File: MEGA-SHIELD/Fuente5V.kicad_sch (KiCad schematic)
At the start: 11 parts, among them J1 12V

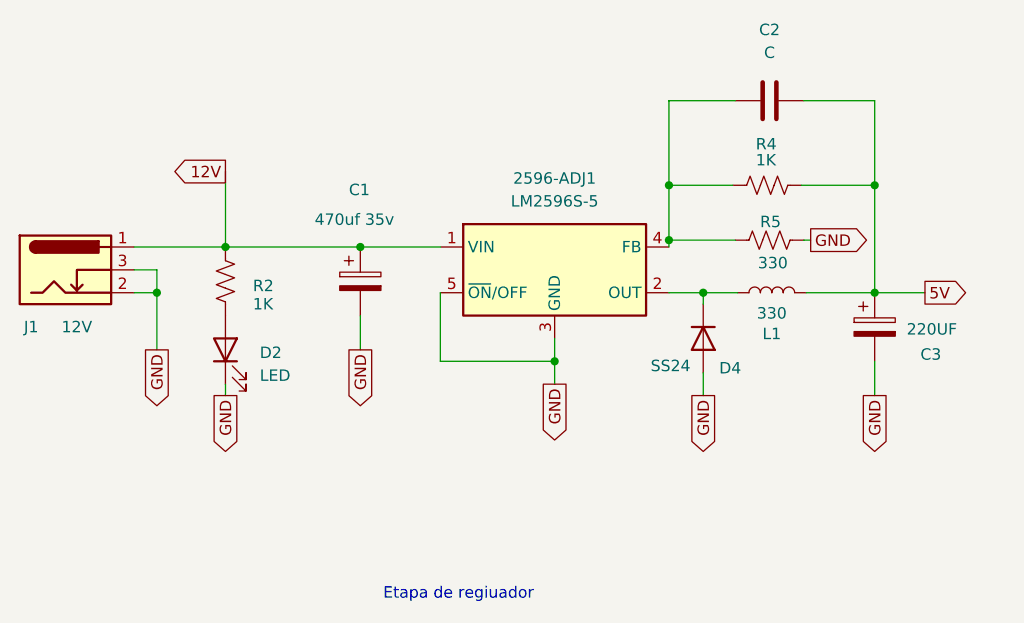
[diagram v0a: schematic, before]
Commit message: feat: agrege reles y optos
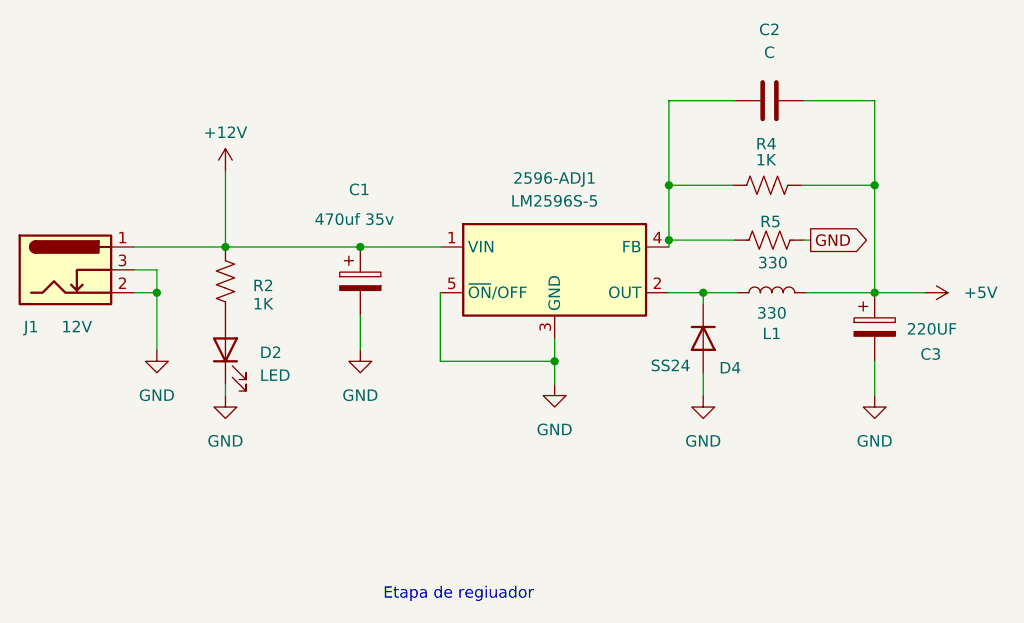
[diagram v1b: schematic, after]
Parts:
- 2596-ADJ1: footprint Package_TO_SOT_SMD:TO-263-5_TabPin3 -> TerminalBlock_Phoenix:TerminalBlock_Phoenix_MPT-0,5-3-2.54_1x03_P2.54mm_Horizontal
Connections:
- net 12V renamed +12V
- net 5V renamed +5V
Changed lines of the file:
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@@
     (effects (font (size 1.27 1.27)) (justify left bottom))
-  )
-  (global_label "GND" (shape output) (at 183.134 113.03 270) (fields_autoplaced)
-    (effects (font (size 1.27 1.27)) (justify right))
-    (property "Intersheetrefs" "${INTERSHEET_REFS}" (at 183.134 119.8063 90)
-      (effects (font (size 1.27 1.27)) (justify right) hide)
-    )
-  )
-  (global_label "GND" (shape output) (at 103.378 107.95 270) (fields_autoplaced)
-    (effects (font (size 1.27 1.27)) (justify right))
-    (property "Intersheetrefs" "${INTERSHEET_REFS}" (at 103.378 114.7263 90)
-      (effects (font (size 1.27 1.27)) (justify right) hide)
-    )
-  )
-  (global_label "5V" (shape output) (at 188.722 101.6 0) (fields_autoplaced)
-    (effects (font (size 1.27 1.27)) (justify left))
-    (property "Intersheetrefs" "${INTERSHEET_REFS}" (at 193.9259 101.6 0)
-      (effects (font (size 1.27 1.27)) (justify left) hide)
-    )
-  )
-  (global_label "GND" (shape output) (at 125.984 107.95 270) (fields_autoplaced)
-    (effects (font (size 1.27 1.27)) (justify right))
-    (property "Intersheetrefs" "${INTERSHEET_REFS}" (at 125.984 114.7263 90)
-      (effects (font (size 1.27 1.27)) (justify right) hide)
-    )
-  )
-  (global_label "GND" (shape output) (at 164.084 113.03 270) (fields_autoplaced)
-    (effects (font (size 1.27 1.27)) (justify right))
-    (property "Intersheetrefs" "${INTERSHEET_REFS}" (at 164.084 119.8063 90)
-      (effects (font (size 1.27 1.27)) (justify right) hide)
-    )
   )
   (global_label "GND" (shape output) (at 176.022 95.758 0) (fields_autoplaced)
@@
     )
   )
-  (global_label "GND" (shape output) (at 110.998 113.03 270) (fields_autoplaced)
-    (effects (font (size 1.27 1.27)) (justify right))
-    (property "Intersheetrefs" "${INTERSHEET_REFS}" (at 110.998 119.8063 90)
-      (effects (font (size 1.27 1.27)) (justify right) hide)
-    )
-  )
-  (global_label "GND" (shape output) (at 147.574 111.76 270) (fields_autoplaced)
-    (effects (font (size 1.27 1.27)) (justify right))
-    (property "Intersheetrefs" "${INTERSHEET_REFS}" (at 147.574 118.5363 90)
-      (effects (font (size 1.27 1.27)) (justify right) hide)
-    )
-  )
-  (global_label "12V" (shape output) (at 110.998 88.138 180) (fields_autoplaced)
-    (effects (font (size 1.27 1.27)) (justify right))
-    (property "Intersheetrefs" "${INTERSHEET_REFS}" (at 104.5846 88.138 0)
-      (effects (font (size 1.27 1.27)) (justify right) hide)
-    )
-  )
   (symbol (lib_id "Device:LED") (at 110.998 107.95 90) (unit 1)
     (in_bom yes) (on_board yes) (dnp no)
@@
     )
   )
+  (symbol (lib_id "power:+12V") (at 110.998 88.138 0) (unit 1)
+    (in_bom yes) (on_board yes) (dnp no) (fields_autoplaced)
+    (property "Reference" "#PWR05" (at 110.998 91.948 0)
+      (effects (font (size 1.27 1.27)) hide)
+    )
+    (property "Value" "+12V" (at 110.998 83.82 0)
+      (effects (font (size 1.27 1.27)))
+    )
+    (property "Footprint" "" (at 110.998 88.138 0)
+      (effects (font (size 1.27 1.27)) hide)
+    )
+    (property "Datasheet" "" (at 110.998 88.138 0)
+      (effects (font (size 1.27 1.27)) hide)
+    )
+    (pin "1")
+    (instances
+      (project "ER-PROMEGA-SHIELD"
+        (path "/8147067b-5845-4831-8ba1-364ec5fe594c/5356d373-8a97-48f5-aa7a-74c7e25ebf78"
+          (reference "#PWR05") (unit 1)
+        )
+      )
+    )
+  )
   (symbol (lib_id "Device:C") (at 171.45 80.264 90) (unit 1)
     (in_bom yes) (on_board yes) (dnp no) (fields_autoplaced)
@@
     )
   )
+  (symbol (lib_id "power:GND") (at 110.998 113.03 0) (unit 1)
+    (in_bom yes) (on_board yes) (dnp no) (fields_autoplaced)
+    (property "Reference" "#PWR07" (at 110.998 119.38 0)
+      (effects (font (size 1.27 1.27)) hide)
+    )
+    (property "Value" "GND" (at 110.998 118.11 0)
+      (effects (font (size 1.27 1.27)))
+    )
+    (property "Footprint" "" (at 110.998 113.03 0)
+      (effects (font (size 1.27 1.27)) hide)
+    )
+    (property "Datasheet" "" (at 110.998 113.03 0)
+      (effects (font (size 1.27 1.27)) hide)
+    )
+    (pin "1")
+    (instances
+      (project "ER-PROMEGA-SHIELD"
+        (path "/8147067b-5845-4831-8ba1-364ec5fe594c/5356d373-8a97-48f5-aa7a-74c7e25ebf78"
+          (reference "#PWR07") (unit 1)
+        )
+      )
+    )
+  )
   (symbol (lib_id "Device:R_US") (at 171.196 89.662 270) (unit 1)
     (in_bom yes) (on_board yes) (dnp no)
@@
     )
   )
+  (symbol (lib_id "power:GND") (at 147.574 111.76 0) (unit 1)
+    (in_bom yes) (on_board yes) (dnp no) (fields_autoplaced)
+    (property "Reference" "#PWR09" (at 147.574 118.11 0)
+      (effects (font (size 1.27 1.27)) hide)
+    )
+    (property "Value" "GND" (at 147.574 116.84 0)
+      (effects (font (size 1.27 1.27)))
+    )
+    (property "Footprint" "" (at 147.574 111.76 0)
+      (effects (font (size 1.27 1.27)) hide)
+    )
+    (property "Datasheet" "" (at 147.574 111.76 0)
+      (effects (font (size 1.27 1.27)) hide)
+    )
+    (pin "1")
+    (instances
+      (project "ER-PROMEGA-SHIELD"
+        (path "/8147067b-5845-4831-8ba1-364ec5fe594c/5356d373-8a97-48f5-aa7a-74c7e25ebf78"
+          (reference "#PWR09") (unit 1)
+        )
+      )
+    )
+  )
   (symbol (lib_id "Regulator_Switching:LM2596S-5") (at 147.574 99.06 0) (unit 1)
     (in_bom yes) (on_board yes) (dnp no) (fields_autoplaced)
@@
       (effects (font (size 1.27 1.27)))
     )
-    (property "Footprint" "Package_TO_SOT_SMD:TO-263-5_TabPin3" (at 148.844 105.41 0)
+    (property "Footprint" "TerminalBlock_Phoenix:TerminalBlock_Phoenix_MPT-0,5-3-2.54_1x03_P2.54mm_Horizontal" (at 148.844 105.41 0)
       (effects (font (size 1.27 1.27) italic) (justify left) hide)
     )
@@
     )
   )
+  (symbol (lib_id "power:+5V") (at 188.722 101.6 270) (unit 1)
+    (in_bom yes) (on_board yes) (dnp no) (fields_autoplaced)
+    (property "Reference" "#PWR012" (at 184.912 101.6 0)
+      (effects (font (size 1.27 1.27)) hide)
+    )
+    (property "Value" "+5V" (at 193.04 101.6 90)
+      (effects (font (size 1.27 1.27)) (justify left))
+    )
+    (property "Footprint" "" (at 188.722 101.6 0)
+      (effects (font (size 1.27 1.27)) hide)
+    )
+    (property "Datasheet" "" (at 188.722 101.6 0)
+      (effects (font (size 1.27 1.27)) hide)
+    )
+    (pin "1")
+    (instances
+      (project "ER-PROMEGA-SHIELD"
+        (path "/8147067b-5845-4831-8ba1-364ec5fe594c/5356d373-8a97-48f5-aa7a-74c7e25ebf78"
+          (reference "#PWR012") (unit 1)
+        )
+      )
+    )
+  )
+  (symbol (lib_id "power:GND") (at 125.984 107.95 0) (unit 1)
+    (in_bom yes) (on_board yes) (dnp no) (fields_autoplaced)
+    (property "Reference" "#PWR08" (at 125.984 114.3 0)
+      (effects (font (size 1.27 1.27)) hide)
+    )
+    (property "Value" "GND" (at 125.984 113.03 0)
+      (effects (font (size 1.27 1.27)))
+    )
+    (property "Footprint" "" (at 125.984 107.95 0)
+      (effects (font (size 1.27 1.27)) hide)
+    )
+    (property "Datasheet" "" (at 125.984 107.95 0)
+      (effects (font (size 1.27 1.27)) hide)
+    )
+    (pin "1")
+    (instances
+      (project "ER-PROMEGA-SHIELD"
+        (path "/8147067b-5845-4831-8ba1-364ec5fe594c/5356d373-8a97-48f5-aa7a-74c7e25ebf78"
+          (reference "#PWR08") (unit 1)
+        )
+      )
+    )
+  )
+  (symbol (lib_id "power:GND") (at 103.378 107.95 0) (unit 1)
+    (in_bom yes) (on_board yes) (dnp no) (fields_autoplaced)
+    (property "Reference" "#PWR06" (at 103.378 114.3 0)
+      (effects (font (size 1.27 1.27)) hide)
+    )
+    (property "Value" "GND" (at 103.378 113.03 0)
+      (effects (font (size 1.27 1.27)))
+    )
+    (property "Footprint" "" (at 103.378 107.95 0)
+      (effects (font (size 1.27 1.27)) hide)
+    )
+    (property "Datasheet" "" (at 103.378 107.95 0)
+      (effects (font (size 1.27 1.27)) hide)
+    )
+    (pin "1")
+    (instances
+      (project "ER-PROMEGA-SHIELD"
+        (path "/8147067b-5845-4831-8ba1-364ec5fe594c/5356d373-8a97-48f5-aa7a-74c7e25ebf78"
+          (reference "#PWR06") (unit 1)
+        )
+      )
+    )
+  )
+  (symbol (lib_id "power:GND") (at 164.084 113.03 0) (unit 1)
+    (in_bom yes) (on_board yes) (dnp no) (fields_autoplaced)
+    (property "Reference" "#PWR010" (at 164.084 119.38 0)
+      (effects (font (size 1.27 1.27)) hide)
+    )
+    (property "Value" "GND" (at 164.084 118.11 0)
+      (effects (font (size 1.27 1.27)))
+    )
+    (property "Footprint" "" (at 164.084 113.03 0)
+      (effects (font (size 1.27 1.27)) hide)
+    )
+    (property "Datasheet" "" (at 164.084 113.03 0)
+      (effects (font (size 1.27 1.27)) hide)
+    )
+    (pin "1")
+    (instances
+      (project "ER-PROMEGA-SHIELD"
+        (path "/8147067b-5845-4831-8ba1-364ec5fe594c/5356d373-8a97-48f5-aa7a-74c7e25ebf78"
+          (reference "#PWR010") (unit 1)
+        )
+      )
+    )
+  )
   (symbol (lib_id "Device:C_Polarized") (at 183.134 105.41 0) (unit 1)
     (in_bom yes) (on_board yes) (dnp no)
@@
         )
       )
+    )
+  )
+  (symbol (lib_id "power:GND") (at 183.134 113.03 0) (unit 1)
+    (in_bom yes) (on_board yes) (dnp no) (fields_autoplaced)
+    (property "Reference" "#PWR011" (at 183.134 119.38 0)
+      (effects (font (size 1.27 1.27)) hide)
+    )
+    (property "Value" "GND" (at 183.134 118.11 0)
+      (effects (font (size 1.27 1.27)))
+    )
+    (property "Footprint" "" (at 183.134 113.03 0)
+      (effects (font (size 1.27 1.27)) hide)
+    )
+    (property "Datasheet" "" (at 183.134 113.03 0)
+      (effects (font (size 1.27 1.27)) hide)
+    )
+    (pin "1")
+    (instances
+      (project "ER-PROMEGA-SHIELD"
+        (path "/8147067b-5845-4831-8ba1-364ec5fe594c/5356d373-8a97-48f5-aa7a-74c7e25ebf78"
+          (reference "#PWR011") (unit 1)
+        )
+      )

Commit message: feat: avances2
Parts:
- 2596-ADJ1: footprint TerminalBlock_Phoenix:TerminalBlock_Phoenix_MPT-0,5-3-2.54_1x03_P2.54mm_Horizontal -> Package_TO_SOT_SMD:TO-263-5_TabPin3
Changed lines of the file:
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@@
       (effects (font (size 1.27 1.27)))
     )
-    (property "Footprint" "TerminalBlock_Phoenix:TerminalBlock_Phoenix_MPT-0,5-3-2.54_1x03_P2.54mm_Horizontal" (at 148.844 105.41 0)
+    (property "Footprint" "Package_TO_SOT_SMD:TO-263-5_TabPin3" (at 148.844 105.41 0)
       (effects (font (size 1.27 1.27) italic) (justify left) hide)
     )

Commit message: develop: version 1.1
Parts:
- 2596-ADJ1: value LM2596S-5 -> REGULADOR ADJ
- R2, R4, R5: footprint Resistor_SMD:R_0805_2012Metric_Pad1.20x1.40mm_HandSolder -> Resistor_SMD:R_0603_1608Metric_Pad0.98x0.95mm_HandSolder
